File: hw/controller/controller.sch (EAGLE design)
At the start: 74 parts, among them J1 JST-PH3SMT_VERT, J2 JST-ZH6, J3 PAD4, J4 JST-PH3SMT_VERT, J5 PAD2, J6 PAD4, Q1 TPN1R603PL, Q2 TPN1R603PL, Q3 TPN1R603PL, Q4 TPN1R603PL, Q5 TPN1R603PL, Q6 TPN1R603PL, U1 STM32F4R_64PIN, U2 DRV8323RS, U3 AS5147, U4 MAX13431E, X1 8.0MHz

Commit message: More random finalizations for board
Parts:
- removed J4: JST-PH3SMT_VERT, controller:JST-PH3SMT_VERT
- added SWD: JST-ZH6, controller:JST-ZH6
- J2: value JST-ZH6 -> JST-PH3SMT_VERT; device controller:JST-ZH6 -> controller:JST-PH3SMT_VERT
- renumbered J3 to ABS, J5 to TEMP, J6 to DBG
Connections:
- net +3V3: now also SWD.6; no longer J2.6
- net GND: now also J2.3, SWD.4; no longer J2.4, J4.3
- net N$15: now also J2.1; no longer J4.1
- net N$24: now also SWD.2; no longer J2.2
- net N$6: now also SWD.5; no longer J2.5
- net N$7: now also SWD.3; no longer J2.3
- net N$9: now also J2.2; no longer J4.2
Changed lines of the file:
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@@
 </part>
 <part name="GND9" library="supply1" deviceset="GND" device=""/>
-<part name="J2" library="controller" deviceset="JST-ZH6" device=""/>
-<part name="J4" library="controller" deviceset="JST-PH3" device="SMT_VERT" value="JST-PH3SMT_VERT"/>
-<part name="J3" library="controller" deviceset="PAD4" device=""/>
+<part name="SWD" library="controller" deviceset="JST-ZH6" device=""/>
+<part name="J2" library="controller" deviceset="JST-PH3" device="SMT_VERT" value="JST-PH3SMT_VERT"/>
+<part name="ABS" library="controller" deviceset="PAD4" device=""/>
 <part name="GND10" library="supply1" deviceset="GND" device=""/>
 <part name="+3V5" library="supply1" deviceset="+3V3" device=""/>
-<part name="J5" library="controller" deviceset="PAD2" device=""/>
+<part name="TEMP" library="controller" deviceset="PAD2" device=""/>
 <part name="+3V6" library="supply1" deviceset="+3V3" device=""/>
 <part name="GND11" library="supply1" deviceset="GND" device=""/>
@@
 <attribute name="MPN" value="MF-RES-0603-220"/>
 </part>
-<part name="J6" library="controller" deviceset="PAD4" device=""/>
+<part name="DBG" library="controller" deviceset="PAD4" device=""/>
 <part name="GND3" library="supply1" deviceset="GND" device=""/>
 <part name="+3V10" library="supply1" deviceset="+3V3" device=""/>
@@
 </instance>
 <instance part="GND9" gate="1" x="121.92" y="-238.76"/>
-<instance part="J2" gate="A" x="-45.72" y="81.28"/>
-<instance part="J4" gate="A" x="129.54" y="-81.28" rot="MR0"/>
-<instance part="J3" gate="A" x="86.36" y="-185.42" rot="MR0"/>
+<instance part="SWD" gate="A" x="-45.72" y="81.28"/>
+<instance part="J2" gate="A" x="129.54" y="-81.28" rot="MR0"/>
+<instance part="ABS" gate="A" x="86.36" y="-185.42" rot="MR0"/>
 <instance part="GND10" gate="1" x="66.04" y="-200.66"/>
 <instance part="+3V5" gate="G$1" x="66.04" y="-172.72"/>
-<instance part="J5" gate="A" x="228.6" y="-129.54" rot="MR0"/>
+<instance part="TEMP" gate="A" x="228.6" y="-129.54" rot="MR0"/>
 <instance part="+3V6" gate="G$1" x="215.9" y="-119.38"/>
 <instance part="GND11" gate="1" x="215.9" y="-154.94"/>
@@
 <attribute name="MPN" x="208.28" y="-50.8" size="1.778" layer="96" display="off"/>
 </instance>
-<instance part="J6" gate="A" x="-2.54" y="-147.32"/>
+<instance part="DBG" gate="A" x="-2.54" y="-147.32"/>
 <instance part="GND3" gate="1" x="7.62" y="-157.48"/>
 <instance part="+3V10" gate="G$1" x="10.16" y="-132.08"/>
@@
 <wire x1="-27.94" y1="96.52" x2="-27.94" y2="76.2" width="0.1524" layer="91"/>
 <wire x1="-40.64" y1="76.2" x2="-27.94" y2="76.2" width="0.1524" layer="91"/>
-<pinref part="J2" gate="A" pin="6"/>
+<pinref part="SWD" gate="A" pin="6"/>
 </segment>
 <segment>
@@
 <pinref part="+3V5" gate="G$1" pin="+3V3"/>
 <wire x1="66.04" y1="-175.26" x2="66.04" y2="-180.34" width="0.1524" layer="91"/>
-<pinref part="J3" gate="A" pin="1"/>
+<pinref part="ABS" gate="A" pin="1"/>
 <wire x1="66.04" y1="-180.34" x2="81.28" y2="-180.34" width="0.1524" layer="91"/>
 <pinref part="C27" gate="G$1" pin="P$1"/>
@@
 <pinref part="+3V6" gate="G$1" pin="+3V3"/>
 <wire x1="215.9" y1="-121.92" x2="215.9" y2="-127" width="0.1524" layer="91"/>
-<pinref part="J5" gate="A" pin="1"/>
+<pinref part="TEMP" gate="A" pin="1"/>
 <wire x1="215.9" y1="-127" x2="223.52" y2="-127" width="0.1524" layer="91"/>
 </segment>
@@
 </segment>
 <segment>
-<pinref part="J6" gate="A" pin="1"/>
+<pinref part="DBG" gate="A" pin="1"/>
 <pinref part="+3V10" gate="G$1" pin="+3V3"/>
 <wire x1="2.54" y1="-142.24" x2="10.16" y2="-142.24" width="0.1524" layer="91"/>
@@
 <wire x1="-30.48" y1="81.28" x2="-30.48" y2="63.5" width="0.1524" layer="91"/>
 <wire x1="-30.48" y1="81.28" x2="-40.64" y2="81.28" width="0.1524" layer="91"/>
-<pinref part="J2" gate="A" pin="4"/>
+<pinref part="SWD" gate="A" pin="4"/>
 </segment>
 <segment>
@@
 <wire x1="88.9" y1="-96.52" x2="116.84" y2="-96.52" width="0.1524" layer="91"/>
 <wire x1="116.84" y1="-96.52" x2="116.84" y2="-83.82" width="0.1524" layer="91"/>
-<pinref part="J4" gate="A" pin="3"/>
+<pinref part="J2" gate="A" pin="3"/>
 <wire x1="116.84" y1="-83.82" x2="124.46" y2="-83.82" width="0.1524" layer="91"/>
 <pinref part="J1" gate="A" pin="3"/>
@@
 <pinref part="GND10" gate="1" pin="GND"/>
 <wire x1="66.04" y1="-198.12" x2="66.04" y2="-193.04" width="0.1524" layer="91"/>
-<pinref part="J3" gate="A" pin="4"/>
+<pinref part="ABS" gate="A" pin="4"/>
 <wire x1="66.04" y1="-193.04" x2="66.04" y2="-187.96" width="0.1524" layer="91"/>
 <wire x1="66.04" y1="-187.96" x2="81.28" y2="-187.96" width="0.1524" layer="91"/>
@@
 </segment>
 <segment>
-<pinref part="J6" gate="A" pin="4"/>
+<pinref part="DBG" gate="A" pin="4"/>
 <wire x1="2.54" y1="-149.86" x2="7.62" y2="-149.86" width="0.1524" layer="91"/>
 <pinref part="GND3" gate="1" pin="GND"/>
@@
 <wire x1="-22.86" y1="86.36" x2="-40.64" y2="86.36" width="0.1524" layer="91"/>
 <pinref part="U1" gate="G$1" pin="NRST"/>
-<pinref part="J2" gate="A" pin="2"/>
+<pinref part="SWD" gate="A" pin="2"/>
 </segment>
 </net>
@@
 <wire x1="-10.16" y1="78.74" x2="-40.64" y2="78.74" width="0.1524" layer="91"/>
 <pinref part="U1" gate="G$1" pin="PA14/SWCLK"/>
-<pinref part="J2" gate="A" pin="5"/>
+<pinref part="SWD" gate="A" pin="5"/>
 </segment>
 </net>
@@
 <wire x1="-7.62" y1="83.82" x2="-40.64" y2="83.82" width="0.1524" layer="91"/>
 <pinref part="U1" gate="G$1" pin="PA13/SWDIO"/>
-<pinref part="J2" gate="A" pin="3"/>
+<pinref part="SWD" gate="A" pin="3"/>
 </segment>
 </net>
@@
 <net name="DEBUG_TX" class="0">
 <segment>
-<pinref part="J6" gate="A" pin="2"/>
+<pinref part="DBG" gate="A" pin="2"/>
 <wire x1="2.54" y1="-144.78" x2="17.78" y2="-144.78" width="0.1524" layer="91"/>
 <label x="7.62" y="-144.78" size="1.778" layer="95"/>
@@
 <net name="DEBUG_RX" class="0">
 <segment>
-<pinref part="J6" gate="A" pin="3"/>
+<pinref part="DBG" gate="A" pin="3"/>
 <wire x1="2.54" y1="-147.32" x2="17.78" y2="-147.32" width="0.1524" layer="91"/>
 <label x="7.62" y="-147.32" size="1.778" layer="95"/>
@@
 <wire x1="104.14" y1="-83.82" x2="109.22" y2="-83.82" width="0.1524" layer="91"/>
 <wire x1="109.22" y1="-83.82" x2="109.22" y2="-81.28" width="0.1524" layer="91"/>
-<pinref part="J4" gate="A" pin="2"/>
+<pinref part="J2" gate="A" pin="2"/>
 <wire x1="109.22" y1="-81.28" x2="124.46" y2="-81.28" width="0.1524" layer="91"/>
 <pinref part="J1" gate="A" pin="2"/>
@@
 <wire x1="104.14" y1="-76.2" x2="109.22" y2="-76.2" width="0.1524" layer="91"/>
 <wire x1="109.22" y1="-76.2" x2="109.22" y2="-78.74" width="0.1524" layer="91"/>
-<pinref part="J4" gate="A" pin="1"/>
+<pinref part="J2" gate="A" pin="1"/>
 <wire x1="109.22" y1="-78.74" x2="124.46" y2="-78.74" width="0.1524" layer="91"/>
 <pinref part="J1" gate="A" pin="1"/>
@@
 <net name="I2C_ABS_SCL" class="0">
 <segment>
-<pinref part="J3" gate="A" pin="3"/>
+<pinref part="ABS" gate="A" pin="3"/>
 <wire x1="81.28" y1="-185.42" x2="66.04" y2="-185.42" width="0.1524" layer="91"/>
 <label x="63.5" y="-185.42" size="1.778" layer="95"/>
@@
 <net name="I2C_ABS_SDA" class="0">
 <segment>
-<pinref part="J3" gate="A" pin="2"/>
+<pinref part="ABS" gate="A" pin="2"/>
 <wire x1="81.28" y1="-182.88" x2="66.04" y2="-182.88" width="0.1524" layer="91"/>
 <label x="63.5" y="-182.88" size="1.778" layer="95"/>
@@
 <pinref part="R5" gate="G$1" pin="P$1"/>
 <wire x1="215.9" y1="-139.7" x2="215.9" y2="-129.54" width="0.1524" layer="91"/>
-<pinref part="J5" gate="A" pin="2"/>
+<pinref part="TEMP" gate="A" pin="2"/>
 <wire x1="215.9" y1="-129.54" x2="223.52" y2="-129.54" width="0.1524" layer="91"/>
 <wire x1="215.9" y1="-129.54" x2="195.58" y2="-129.54" width="0.1524" layer="91"/>

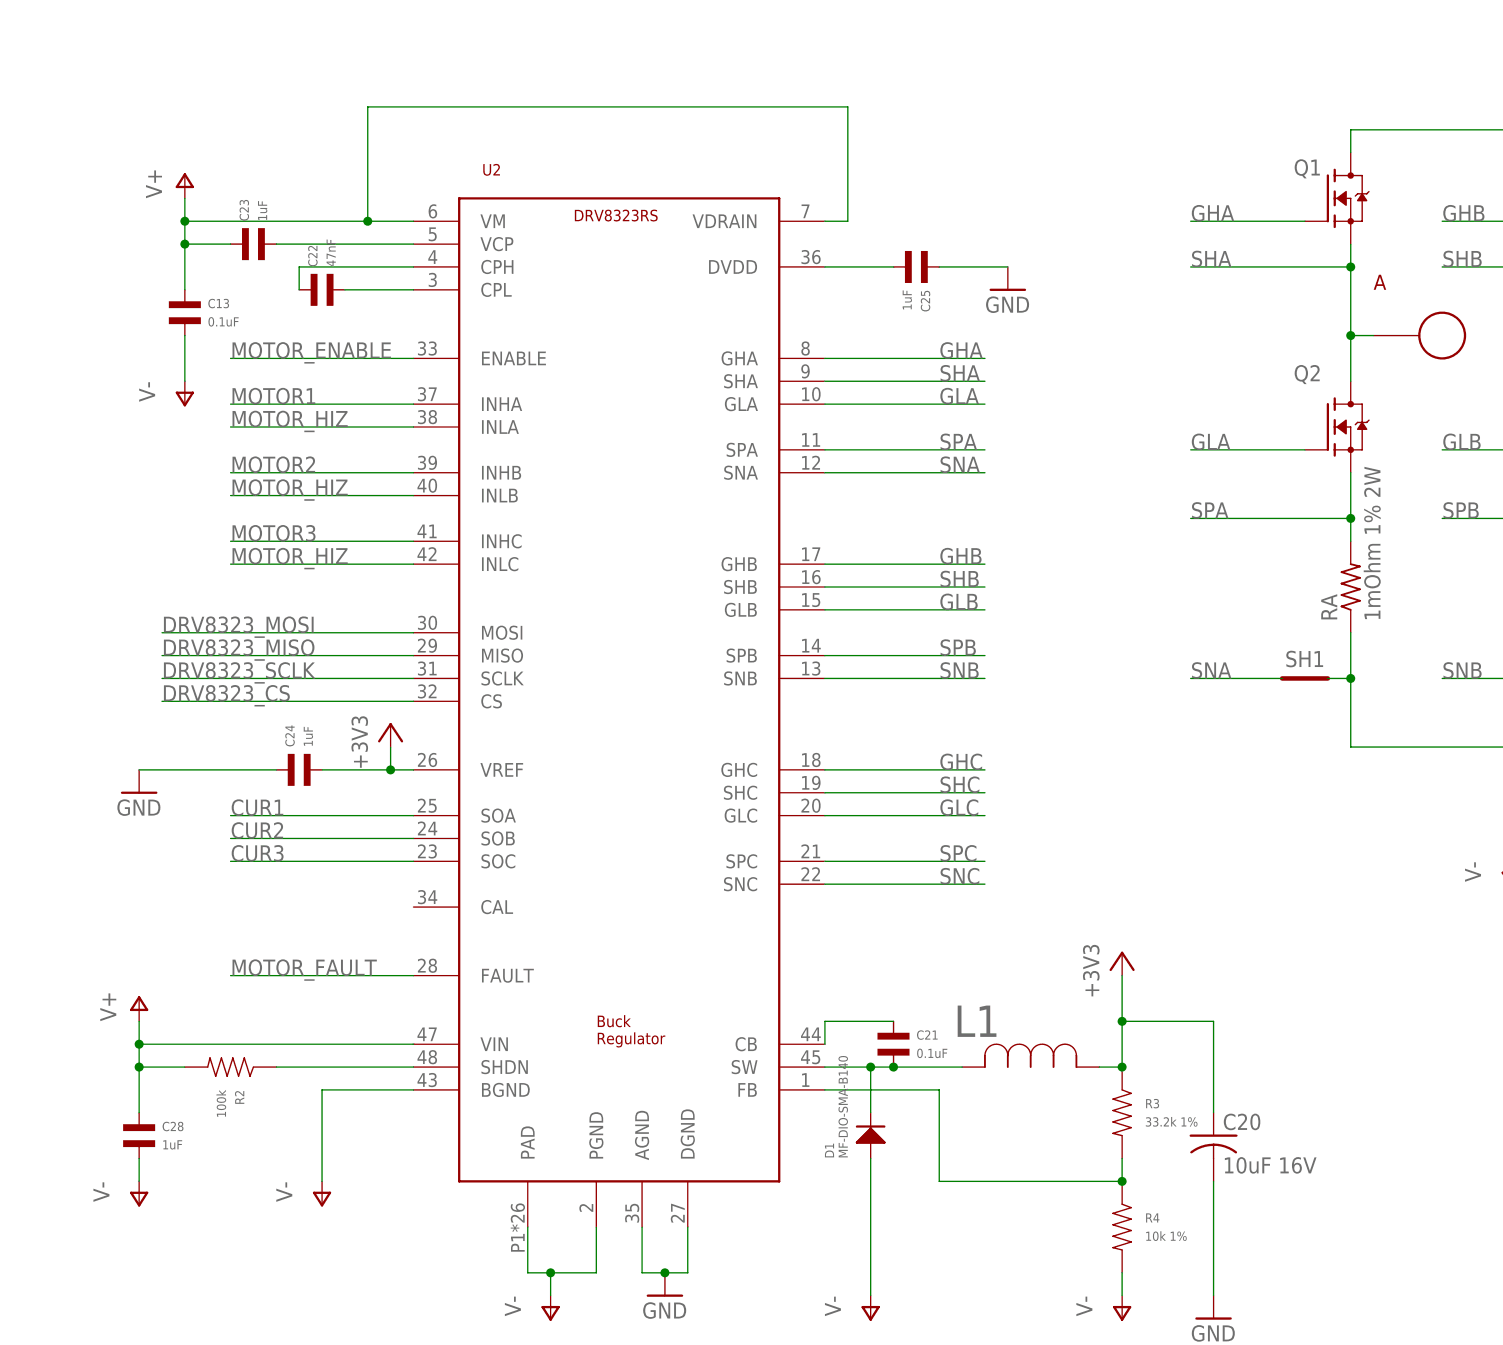
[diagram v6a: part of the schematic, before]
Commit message: Fill in most MPNs
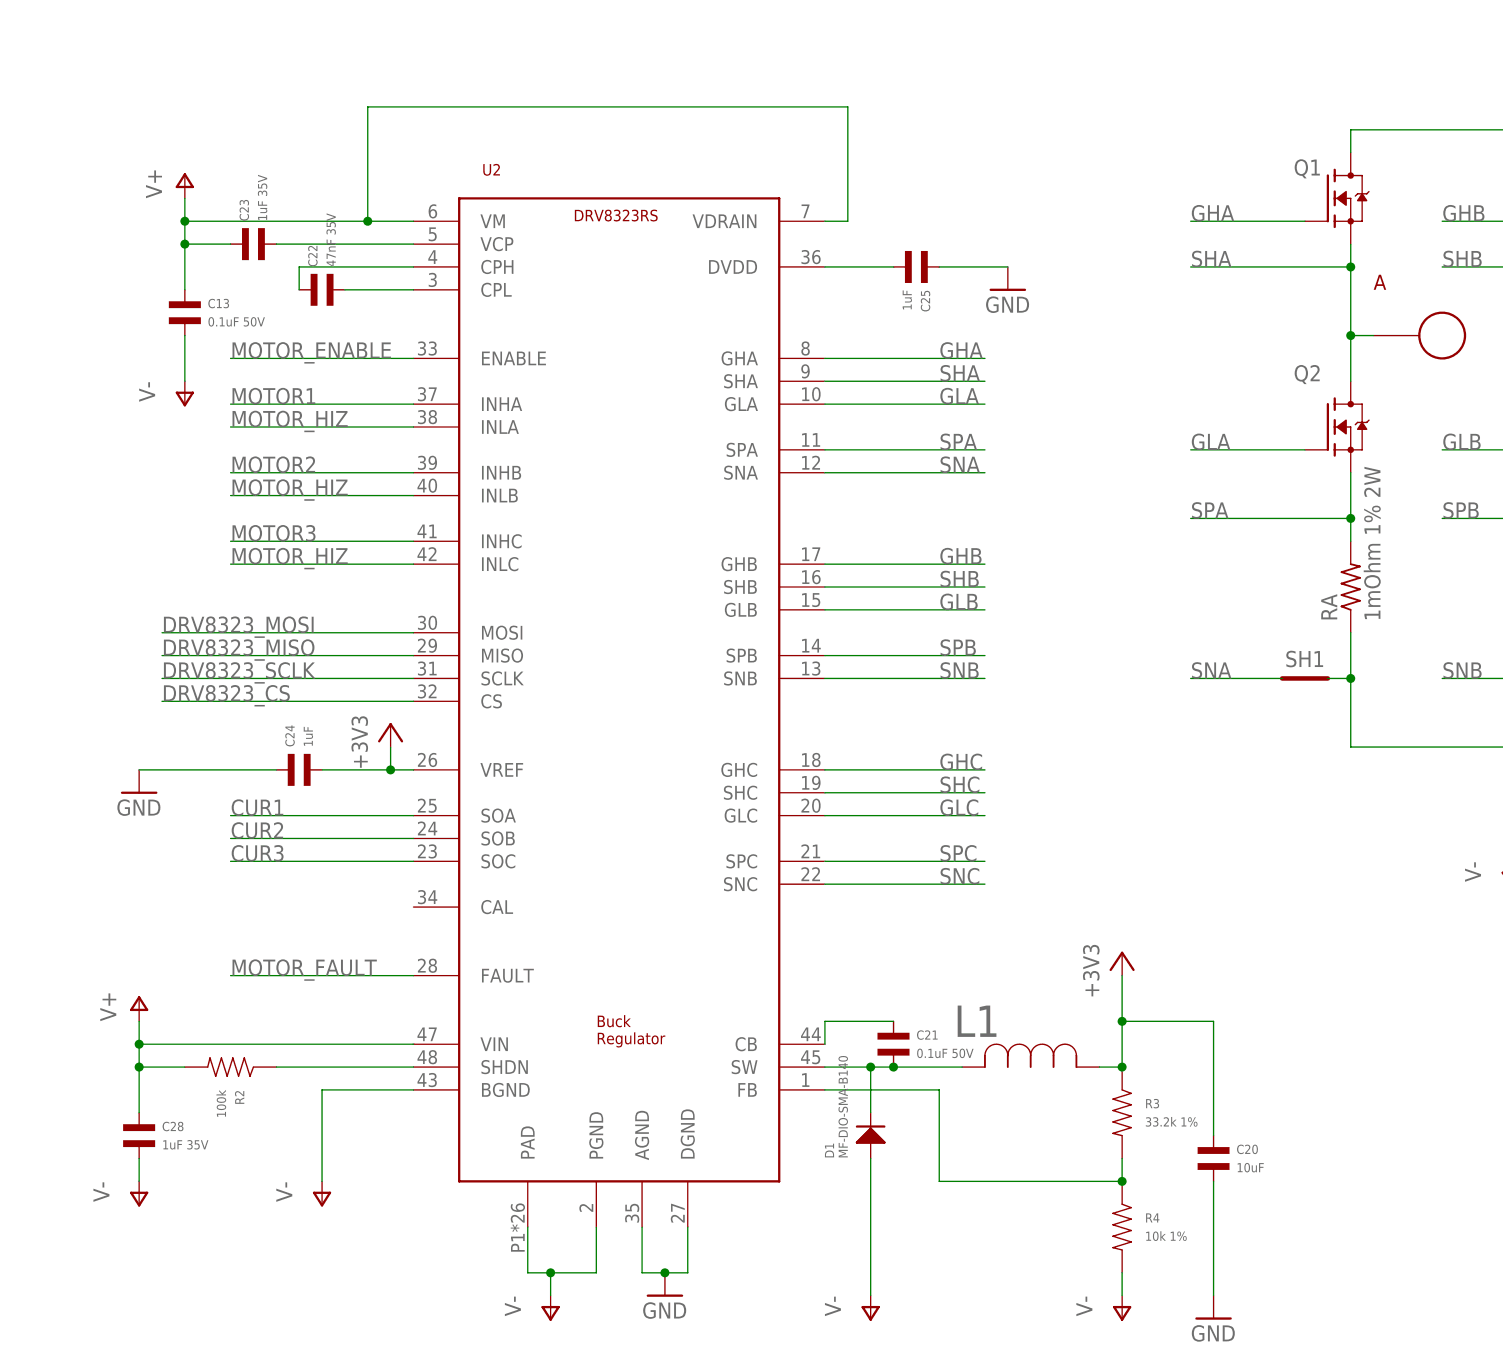
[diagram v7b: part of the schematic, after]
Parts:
- A, ABS, B, C, DBG, SH1, SH2, SH3, SH4, TEMP, U$1, U$2, U$3, U$4, V+, V-: POPULATE (none) -> 0
- C1, C7: DPN 311-1455-1-ND -> (none); MF (none) -> Samsung Electro-Mechanics; MPN CC0603KRX5R6BB475 -> CL10A475MP8NNNC
- C10, C11, C12, C2, C26, C3, C5, C6: HOUSEPART (none) -> 1; MPN MF-CAP-0603-0.1uF -> MF-CAP-0402-0.1uF
- C13, C21: value 0.1uF -> 0.1uF 50V; MF (none) -> TDK; MPN MF-CAP-0603-0.1uF -> C1005X7R1H104K050BE
- C14, C15, C16, C17, C18, C19, L1, RA, RB, RC: POPULATE (none) -> 1
- C20: value 10uF 16V -> 10uF; device rcl:C-USC1206 -> mfpassives:CAPACITOR_NP_1206; HOUSEPART (none) -> 1; MPN (none) -> MF-CAP-1206-10uF
- C22: value 47nF -> 47nF 35V; MF (none) -> TDK; MPN (none) -> CGA2B3X5R1V473K050BB
- C23: value 1uF -> 1uF 35V; MF (none) -> Samsung Electro-Mechanics; MPN MF-CAP-0603-1uF -> CL05A105KL5NRNC
- C24, C25: HOUSEPART (none) -> 1; MPN MF-CAP-0603-1uF -> MF-CAP-0402-1uF
- C28: value 1uF -> 1uF 35V; MF (none) -> Samsung Electro-Mechanics; MPN MF-CAP-0402-1uF -> CL05A105KL5NRNC
- C8, C9: HOUSEPART (none) -> 1; MPN MF-CAP-0603-10pF -> MF-CAP-0402-10pF
- J1, J2: MF (none) -> JST; MPN (none) -> B3B-PH-SM4-TB(LF)(SN); POPULATE (none) -> 1
- Q1, Q2, Q3, Q4, Q5, Q6: MF (none) -> Toshiba; MPN (none) -> TPN1R603PL,L1Q; POPULATE (none) -> 1
- R2: DPN P100KHCT-ND -> (none); HOUSEPART (none) -> 1; MPN ERJ-3EKF1003V -> MF-RES-0402-100K
- R5: HOUSEPART (none) -> 1; MPN MF-RES-0603-10K -> MF-RES-0402-10K
- R6, R9: HOUSEPART (none) -> 1; MPN MF-RES-0603-220 -> MF-RES-0402-220
- SWD: MF (none) -> JST; MPN (none) -> S6B-ZR-SM4A-TF(LF)(SN); POPULATE (none) -> 1
- U1: MF (none) -> ST; MPN (none) -> STM32F446RET6; POPULATE (none) -> 1
- U2: MF (none) -> TI; MPN (none) -> DRV8323RSRGZR; POPULATE (none) -> 1
- U3: MF (none) -> AMS; MPN (none) -> AS5047P-ATSM; POPULATE (none) -> 1
- U4: MF (none) -> Maxim; MPN (none) -> MAX13431EETB+T; POPULATE (none) -> 1
- X1: device gimbal:CRYSTALABM3B -> controller:CRYSTALABM3B; DPN 535-9721-1-ND -> (none); MF (none) -> Abracon; POPULATE (none) -> 1
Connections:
- net +3V3: now also C20.P$1; no longer C20.1
- net GND: now also C20.P$2; no longer C20.2

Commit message: Autorouting and final silk placement
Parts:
- R1: HOUSEPART (none) -> 1; MPN MF-RES-0603-10 -> MF-RES-0402-10
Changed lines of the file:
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@@
 <part name="+3V8" library="supply1" deviceset="+3V3" device=""/>
 <part name="R1" library="mfpassives" deviceset="RESISTOR" device="_0402" value="10">
-<attribute name="MPN" value="MF-RES-0603-10"/>
+<attribute name="HOUSEPART" value="1"/>
+<attribute name="MPN" value="MF-RES-0402-10"/>
 </part>
 <part name="C2" library="mfpassives" deviceset="CAPACITOR_NP" device="_0402" value="0.1uF">
